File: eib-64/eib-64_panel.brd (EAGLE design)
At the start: 70.6 x 68 mm, 300 parts, among them J1 DF40-REC, J10 DF40-REC, J11 DF40-REC, J15 DF40-REC, J16 DF40-REC, J17 DF40-REC, J18 DF40-REC, J2 DF40-REC, J3 DF40-REC, J4 DF40-REC, J8 DF40-REC, J9 DF40-REC

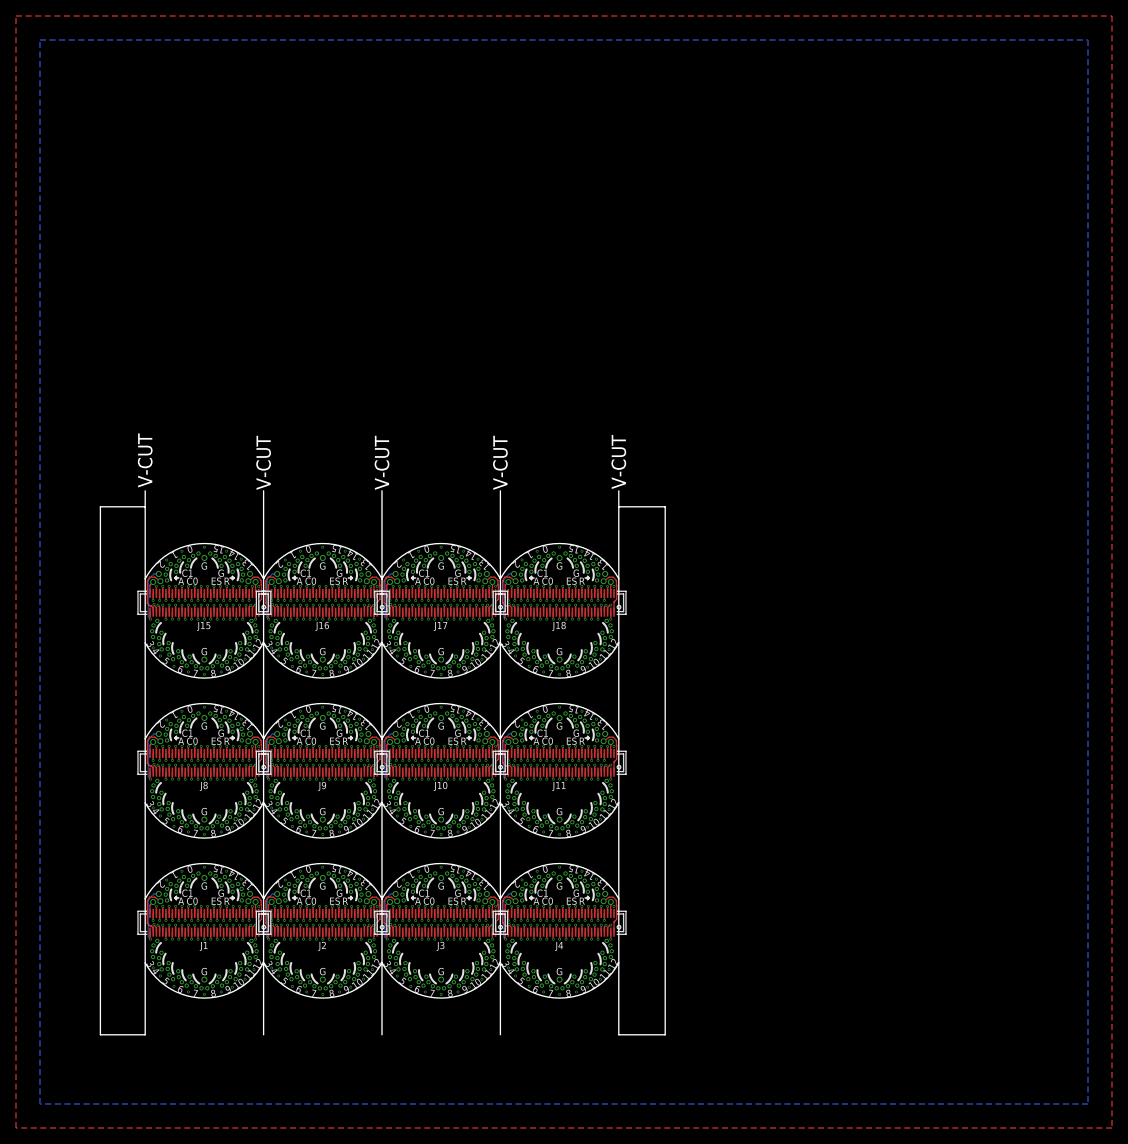
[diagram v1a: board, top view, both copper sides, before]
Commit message: eib-64 rev. 1.1
- Fits latest shuttle drive reatining feature.
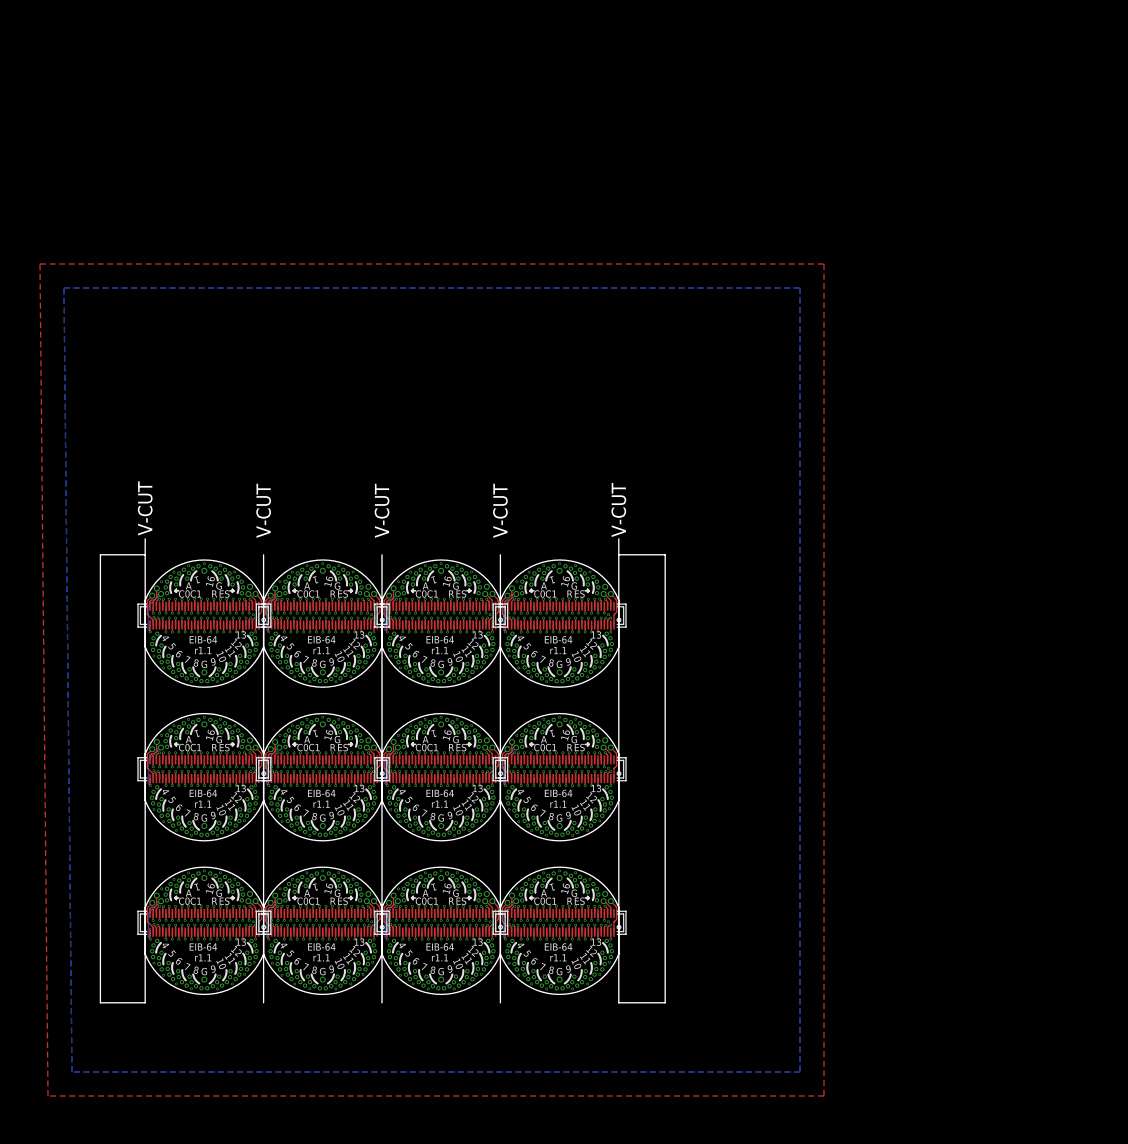
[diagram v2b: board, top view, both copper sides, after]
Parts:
- removed AN14, AN15, AN16, AN17, CAT28, CAT29, CAT30, CAT31, CAT32, CAT33, CAT34, CAT35, ESTIM14, ESTIM15, ESTIM16, ESTIM17, GND2, GND29, GND30, GND31, GND32, GND33, GND34, GND35, REF14, REF15, REF16, REF17, SHLD_A14, SHLD_A15, SHLD_A16, SHLD_A17: LRG_GP, jonnew:GOLDPIN_0.5ID_0.7OD
- removed J15, J16, J17, J18: DF40-REC, jonnew:DF40-70REC
- removed TET224, TET240, TET256, TET272: 0, jonnew:TETRODE_0.3ID_LINEAR_MOUSE
- removed TET225, TET241, TET257, TET273: 1, jonnew:TETRODE_0.3ID_LINEAR_MOUSE
- removed TET226, TET242, TET258, TET274: 2, jonnew:TETRODE_0.3ID_LINEAR_MOUSE
- removed TET227, TET243, TET259, TET275: 3, jonnew:TETRODE_0.3ID_LINEAR_MOUSE
- removed TET228, TET244, TET260, TET276: 4, jonnew:TETRODE_0.3ID_LINEAR_MOUSE
- removed TET229, TET245, TET261, TET277: 5, jonnew:TETRODE_0.3ID_LINEAR_MOUSE
- removed TET230, TET246, TET262, TET278: 6, jonnew:TETRODE_0.3ID_LINEAR_MOUSE
- removed TET231, TET247, TET263, TET279: 7, jonnew:TETRODE_0.3ID_LINEAR_MOUSE
- removed TET232, TET248, TET264, TET280: 15, jonnew:TETRODE_0.3ID_LINEAR_MOUSE
- removed TET233, TET249, TET265, TET281: 14, jonnew:TETRODE_0.3ID_LINEAR_MOUSE
- removed TET234, TET250, TET266, TET282: 13, jonnew:TETRODE_0.3ID_LINEAR_MOUSE
- removed TET235, TET251, TET267, TET283: 12, jonnew:TETRODE_0.3ID_LINEAR_MOUSE
- removed TET236, TET252, TET268, TET284: 11, jonnew:TETRODE_0.3ID_LINEAR_MOUSE
- removed TET237, TET253, TET269, TET285: 10, jonnew:TETRODE_0.3ID_LINEAR_MOUSE
- removed TET238, TET254, TET270, TET286: 9, jonnew:TETRODE_0.3ID_LINEAR_MOUSE
- removed TET239, TET255, TET271, TET287: 8, jonnew:TETRODE_0.3ID_LINEAR_MOUSE
- added AN11, AN4, AN5, AN6, CAT10, CAT11, CAT12, CAT13, CAT22, CAT23, CAT8, CAT9, ESTIM11, ESTIM4, ESTIM5, ESTIM6, GND10, GND11, GND12, GND13, GND22, GND23, GND8, GND9, REF11, REF4, REF5, REF6, SHLD_A11, SHLD_A4, SHLD_A5, SHLD_A6: LRG_GP, jonnew:GOLDPIN_0.5ID_0.7OD
- added J12, J5, J6, J7: DF40-REC, jonnew:DF40-70REC
- added TET100, TET180, TET68, TET84: 4, jonnew:TETRODE_0.3ID_LINEAR_MOUSE
- added TET101, TET181, TET69, TET85: 5, jonnew:TETRODE_0.3ID_LINEAR_MOUSE
- added TET102, TET182, TET70, TET86: 6, jonnew:TETRODE_0.3ID_LINEAR_MOUSE
- added TET103, TET183, TET71, TET87: 7, jonnew:TETRODE_0.3ID_LINEAR_MOUSE
- added TET104, TET184, TET72, TET88: 15, jonnew:TETRODE_0.3ID_LINEAR_MOUSE
- added TET105, TET185, TET73, TET89: 14, jonnew:TETRODE_0.3ID_LINEAR_MOUSE
- added TET106, TET186, TET74, TET90: 13, jonnew:TETRODE_0.3ID_LINEAR_MOUSE
- added TET107, TET187, TET75, TET91: 12, jonnew:TETRODE_0.3ID_LINEAR_MOUSE
- added TET108, TET188, TET76, TET92: 11, jonnew:TETRODE_0.3ID_LINEAR_MOUSE
- added TET109, TET189, TET77, TET93: 10, jonnew:TETRODE_0.3ID_LINEAR_MOUSE
- added TET110, TET190, TET78, TET94: 9, jonnew:TETRODE_0.3ID_LINEAR_MOUSE
- added TET111, TET191, TET79, TET95: 8, jonnew:TETRODE_0.3ID_LINEAR_MOUSE
- added TET176, TET64, TET80, TET96: 0, jonnew:TETRODE_0.3ID_LINEAR_MOUSE
- added TET177, TET65, TET81, TET97: 1, jonnew:TETRODE_0.3ID_LINEAR_MOUSE
- added TET178, TET66, TET82, TET98: 2, jonnew:TETRODE_0.3ID_LINEAR_MOUSE
- added TET179, TET67, TET83, TET99: 3, jonnew:TETRODE_0.3ID_LINEAR_MOUSE
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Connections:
- removed net AN14: AN14.P$1, J15.36
- removed net AN15: AN15.P$1, J16.36
- removed net AN16: AN16.P$1, J17.36
- removed net AN17: AN17.P$1, J18.36
- removed net CAT28: CAT28.P$1, J15.34
- removed net CAT29: CAT29.P$1, J15.35
- removed net CAT30: CAT30.P$1, J16.34
- removed net CAT31: CAT31.P$1, J16.35
- removed net CAT32: CAT32.P$1, J17.34
- removed net CAT33: CAT33.P$1, J17.35
- removed net CAT34: CAT34.P$1, J18.34
- removed net CAT35: CAT35.P$1, J18.35
- removed net ESTIM14: ESTIM14.P$1, J15.1
- removed net ESTIM15: ESTIM15.P$1, J16.1
- removed net ESTIM16: ESTIM16.P$1, J17.1
- removed net ESTIM17: ESTIM17.P$1, J18.1
- removed net N$1000: J16.55, TET248.1
- removed net N$1001: J16.54, TET248.2
- removed net N$1002: J16.53, TET248.3
- removed net N$1003: J16.52, TET240.3
- removed net N$1004: J16.51, TET240.2
- removed net N$1005: J16.50, TET240.1
- removed net N$1006: J16.49, TET240.0
- removed net N$1007: J16.48, TET241.3
- removed net N$1008: J16.47, TET241.2
- removed net N$1009: J16.46, TET241.1
- removed net N$1010: J16.45, TET241.0
- removed net N$1011: J16.44, TET242.3
- removed net N$1012: J16.43, TET242.2
- removed net N$1013: J16.42, TET242.1
- removed net N$1014: J16.41, TET242.0
- removed net N$1015: J16.40, TET243.0
- removed net N$1016: J16.38, TET243.2
- removed net N$1017: J16.5, TET252.3
- removed net N$1018: J16.4, TET252.2
- removed net N$1019: J16.3, TET252.1
- removed net N$1020: J16.2, TET252.0
- removed net N$1021: J16.65, TET251.2
- removed net N$1022: J16.67, TET251.0
- removed net N$1023: J16.39, TET243.3
- removed net N$1024: J16.37, TET243.1
- removed net N$1025: J17.33, TET260.0
- removed net N$1026: J17.32, TET260.1
- removed net N$1027: J17.31, TET260.2
- removed net N$1028: J17.30, TET260.3
- removed net N$1029: J17.29, TET261.0
- removed net N$1030: J17.28, TET261.1
- removed net N$1031: J17.27, TET261.2
- removed net N$1032: J17.26, TET261.3
- removed net N$1033: J17.25, TET262.0
- removed net N$1034: J17.24, TET262.1
- removed net N$1035: J17.23, TET262.2
- removed net N$1036: J17.22, TET262.3
- removed net N$1037: J17.21, TET263.0
- removed net N$1038: J17.20, TET263.1
- removed net N$1039: J17.19, TET263.2
- removed net N$1040: J17.18, TET263.3
- removed net N$1041: J17.17, TET271.3
- removed net N$1042: J17.16, TET271.2
- removed net N$1043: J17.15, TET271.1
- removed net N$1044: J17.14, TET271.0
- removed net N$1045: J17.13, TET270.3
- removed net N$1046: J17.12, TET270.2
- removed net N$1047: J17.11, TET270.1
- removed net N$1048: J17.10, TET270.0
- removed net N$1049: J17.9, TET269.3
- removed net N$1050: J17.8, TET269.2
- removed net N$1051: J17.7, TET269.1
- removed net N$1052: J17.6, TET269.0
- removed net N$1053: J17.68, TET267.3
- removed net N$1054: J17.66, TET267.1
- removed net N$1055: J17.64, TET266.0
- removed net N$1056: J17.63, TET266.1
- removed net N$1057: J17.62, TET266.2
- removed net N$1058: J17.61, TET266.3
- removed net N$1059: J17.60, TET265.0
- removed net N$1060: J17.59, TET265.1
- removed net N$1061: J17.58, TET265.2
- removed net N$1062: J17.57, TET265.3
- removed net N$1063: J17.56, TET264.0
- removed net N$1064: J17.55, TET264.1
- removed net N$1065: J17.54, TET264.2
- removed net N$1066: J17.53, TET264.3
- removed net N$1067: J17.52, TET256.3
- removed net N$1068: J17.51, TET256.2
- removed net N$1069: J17.50, TET256.1
- removed net N$1070: J17.49, TET256.0
- removed net N$1071: J17.48, TET257.3
- removed net N$1072: J17.47, TET257.2
- removed net N$1073: J17.46, TET257.1
- removed net N$1074: J17.45, TET257.0
- removed net N$1075: J17.44, TET258.3
- removed net N$1076: J17.43, TET258.2
- removed net N$1077: J17.42, TET258.1
- removed net N$1078: J17.41, TET258.0
- removed net N$1079: J17.40, TET259.0
- removed net N$1080: J17.38, TET259.2
- removed net N$1081: J17.5, TET268.3
- removed net N$1082: J17.4, TET268.2
- removed net N$1083: J17.3, TET268.1
- removed net N$1084: J17.2, TET268.0
- removed net N$1085: J17.65, TET267.2
- removed net N$1086: J17.67, TET267.0
- removed net N$1087: J17.39, TET259.3
- removed net N$1088: J17.37, TET259.1
- removed net N$1089: J18.33, TET276.0
- removed net N$1090: J18.32, TET276.1
- removed net N$1091: J18.31, TET276.2
- removed net N$1092: J18.30, TET276.3
- removed net N$1093: J18.29, TET277.0
- removed net N$1094: J18.28, TET277.1
- removed net N$1095: J18.27, TET277.2
- removed net N$1096: J18.26, TET277.3
- removed net N$1097: J18.25, TET278.0
- removed net N$1098: J18.24, TET278.1
- removed net N$1099: J18.23, TET278.2
- removed net N$1100: J18.22, TET278.3
- removed net N$1101: J18.21, TET279.0
- removed net N$1102: J18.20, TET279.1
- removed net N$1103: J18.19, TET279.2
- removed net N$1104: J18.18, TET279.3
- removed net N$1105: J18.17, TET287.3
- removed net N$1106: J18.16, TET287.2
- removed net N$1107: J18.15, TET287.1
- removed net N$1108: J18.14, TET287.0
- removed net N$1109: J18.13, TET286.3
- removed net N$1110: J18.12, TET286.2
- removed net N$1111: J18.11, TET286.1
- removed net N$1112: J18.10, TET286.0
- removed net N$1113: J18.9, TET285.3
- removed net N$1114: J18.8, TET285.2
- removed net N$1115: J18.7, TET285.1
- removed net N$1116: J18.6, TET285.0
- removed net N$1117: J18.68, TET283.3
- removed net N$1118: J18.66, TET283.1
- removed net N$1119: J18.64, TET282.0
- removed net N$1120: J18.63, TET282.1
- removed net N$1121: J18.62, TET282.2
- removed net N$1122: J18.61, TET282.3
- removed net N$1123: J18.60, TET281.0
- removed net N$1124: J18.59, TET281.1
- removed net N$1125: J18.58, TET281.2
- removed net N$1126: J18.57, TET281.3
- removed net N$1127: J18.56, TET280.0
- removed net N$1128: J18.55, TET280.1
- removed net N$1129: J18.54, TET280.2
- removed net N$1130: J18.53, TET280.3
- removed net N$1131: J18.52, TET272.3
- removed net N$1132: J18.51, TET272.2
- removed net N$1133: J18.50, TET272.1
- removed net N$1134: J18.49, TET272.0
- removed net N$1135: J18.48, TET273.3
- removed net N$1136: J18.47, TET273.2
- removed net N$1137: J18.46, TET273.1
- removed net N$1138: J18.45, TET273.0
- removed net N$1139: J18.44, TET274.3
- removed net N$1140: J18.43, TET274.2
- removed net N$1141: J18.42, TET274.1
- removed net N$1142: J18.41, TET274.0
- removed net N$1143: J18.40, TET275.0
- removed net N$1144: J18.38, TET275.2
- removed net N$1145: J18.5, TET284.3
- removed net N$1146: J18.4, TET284.2
- removed net N$1147: J18.3, TET284.1
- removed net N$1148: J18.2, TET284.0
- removed net N$1149: J18.65, TET283.2
- removed net N$1150: J18.67, TET283.0
- removed net N$1151: J18.39, TET275.3
- removed net N$1152: J18.37, TET275.1
- removed net N$897: J15.33, TET228.0
- removed net N$898: J15.32, TET228.1
- removed net N$899: J15.31, TET228.2
- removed net N$900: J15.30, TET228.3
- removed net N$901: J15.29, TET229.0
- removed net N$902: J15.28, TET229.1
- removed net N$903: J15.27, TET229.2
- removed net N$904: J15.26, TET229.3
- removed net N$905: J15.25, TET230.0
- removed net N$906: J15.24, TET230.1
- removed net N$907: J15.23, TET230.2
- removed net N$908: J15.22, TET230.3
- removed net N$909: J15.21, TET231.0
- removed net N$910: J15.20, TET231.1
- removed net N$911: J15.19, TET231.2
- removed net N$912: J15.18, TET231.3
- removed net N$913: J15.17, TET239.3
- removed net N$914: J15.16, TET239.2
- removed net N$915: J15.15, TET239.1
- removed net N$916: J15.14, TET239.0
- removed net N$917: J15.13, TET238.3
- removed net N$918: J15.12, TET238.2
- removed net N$919: J15.11, TET238.1
- removed net N$920: J15.10, TET238.0
- removed net N$921: J15.9, TET237.3
- removed net N$922: J15.8, TET237.2
- removed net N$923: J15.7, TET237.1
- removed net N$924: J15.6, TET237.0
- removed net N$925: J15.68, TET235.3
- removed net N$926: J15.66, TET235.1
- removed net N$927: J15.64, TET234.0
- removed net N$928: J15.63, TET234.1
- removed net N$929: J15.62, TET234.2
- removed net N$930: J15.61, TET234.3
- removed net N$931: J15.60, TET233.0
- removed net N$932: J15.59, TET233.1
- removed net N$933: J15.58, TET233.2
- removed net N$934: J15.57, TET233.3
- removed net N$935: J15.56, TET232.0
- removed net N$936: J15.55, TET232.1
- removed net N$937: J15.54, TET232.2
- removed net N$938: J15.53, TET232.3
- removed net N$939: J15.52, TET224.3
- removed net N$940: J15.51, TET224.2
- removed net N$941: J15.50, TET224.1
- removed net N$942: J15.49, TET224.0
- removed net N$943: J15.48, TET225.3
- removed net N$944: J15.47, TET225.2
- removed net N$945: J15.46, TET225.1
- removed net N$946: J15.45, TET225.0
- removed net N$947: J15.44, TET226.3
- removed net N$948: J15.43, TET226.2
- removed net N$949: J15.42, TET226.1
- removed net N$950: J15.41, TET226.0
- removed net N$951: J15.40, TET227.0
- removed net N$952: J15.38, TET227.2
- removed net N$953: J15.5, TET236.3
- removed net N$954: J15.4, TET236.2
- removed net N$955: J15.3, TET236.1
- removed net N$956: J15.2, TET236.0
- removed net N$957: J15.65, TET235.2
- removed net N$958: J15.67, TET235.0
- removed net N$959: J15.39, TET227.3
- removed net N$960: J15.37, TET227.1
- removed net N$961: J16.33, TET244.0
- removed net N$962: J16.32, TET244.1
- removed net N$963: J16.31, TET244.2
- removed net N$964: J16.30, TET244.3
- removed net N$965: J16.29, TET245.0
- removed net N$966: J16.28, TET245.1
- removed net N$967: J16.27, TET245.2
- removed net N$968: J16.26, TET245.3
- removed net N$969: J16.25, TET246.0
- removed net N$970: J16.24, TET246.1
- removed net N$971: J16.23, TET246.2
- removed net N$972: J16.22, TET246.3
- removed net N$973: J16.21, TET247.0
- removed net N$974: J16.20, TET247.1
- removed net N$975: J16.19, TET247.2
- removed net N$976: J16.18, TET247.3
- removed net N$977: J16.17, TET255.3
- removed net N$978: J16.16, TET255.2
- removed net N$979: J16.15, TET255.1
- removed net N$980: J16.14, TET255.0
- removed net N$981: J16.13, TET254.3
- removed net N$982: J16.12, TET254.2
- removed net N$983: J16.11, TET254.1
- removed net N$984: J16.10, TET254.0
- removed net N$985: J16.9, TET253.3
- removed net N$986: J16.8, TET253.2
- removed net N$987: J16.7, TET253.1
- removed net N$988: J16.6, TET253.0
- removed net N$989: J16.68, TET251.3
- removed net N$990: J16.66, TET251.1
- removed net N$991: J16.64, TET250.0
- removed net N$992: J16.63, TET250.1
- removed net N$993: J16.62, TET250.2
- removed net N$994: J16.61, TET250.3
- removed net N$995: J16.60, TET249.0
- removed net N$996: J16.59, TET249.1
- removed net N$997: J16.58, TET249.2
- removed net N$998: J16.57, TET249.3
- removed net N$999: J16.56, TET248.0
- removed net REF14: J15.69, REF14.P$1
- removed net REF15: J16.69, REF15.P$1
- removed net REF16: J17.69, REF16.P$1
- removed net REF17: J18.69, REF17.P$1
- new net AN11: AN11.P$1, J12.36
- new net AN4: AN4.P$1, J5.36
- new net AN5: AN5.P$1, J6.36
- new net AN6: AN6.P$1, J7.36
- new net CAT10: CAT10.P$1, J6.34
- new net CAT11: CAT11.P$1, J6.35
- new net CAT12: CAT12.P$1, J7.34
- new net CAT13: CAT13.P$1, J7.35
- new net CAT22: CAT22.P$1, J12.34
- new net CAT23: CAT23.P$1, J12.35
- new net CAT8: CAT8.P$1, J5.34
- new net CAT9: CAT9.P$1, J5.35
- new net ESTIM11: ESTIM11.P$1, J12.1
- new net ESTIM4: ESTIM4.P$1, J5.1
- new net ESTIM5: ESTIM5.P$1, J6.1
- new net ESTIM6: ESTIM6.P$1, J7.1
- new net N$257: J5.33, TET68.0
- new net N$258: J5.32, TET68.1
- new net N$259: J5.31, TET68.2
- new net N$260: J5.30, TET68.3
- new net N$261: J5.29, TET69.0
- new net N$262: J5.28, TET69.1
- new net N$263: J5.27, TET69.2
- new net N$264: J5.26, TET69.3
- new net N$265: J5.25, TET70.0
- new net N$266: J5.24, TET70.1
- new net N$267: J5.23, TET70.2
- new net N$268: J5.22, TET70.3
- new net N$269: J5.21, TET71.0
- new net N$270: J5.20, TET71.1
- new net N$271: J5.19, TET71.2
- new net N$272: J5.18, TET71.3
- new net N$273: J5.17, TET79.3
- new net N$274: J5.16, TET79.2
- new net N$275: J5.15, TET79.1
- new net N$276: J5.14, TET79.0
- new net N$277: J5.13, TET78.3
- new net N$278: J5.12, TET78.2
- new net N$279: J5.11, TET78.1
- new net N$280: J5.10, TET78.0
- new net N$281: J5.9, TET77.3
- new net N$282: J5.8, TET77.2
- new net N$283: J5.7, TET77.1
- new net N$284: J5.6, TET77.0
- new net N$285: J5.68, TET75.3
- new net N$286: J5.66, TET75.1
- new net N$287: J5.64, TET74.0
- new net N$288: J5.63, TET74.1
- new net N$289: J5.62, TET74.2
- new net N$290: J5.61, TET74.3
- new net N$291: J5.60, TET73.0
- new net N$292: J5.59, TET73.1
- new net N$293: J5.58, TET73.2
- new net N$294: J5.57, TET73.3
- new net N$295: J5.56, TET72.0
- new net N$296: J5.55, TET72.1
- new net N$297: J5.54, TET72.2
- new net N$298: J5.53, TET72.3
- new net N$299: J5.52, TET64.3
- new net N$300: J5.51, TET64.2
- new net N$301: J5.50, TET64.1
- new net N$302: J5.49, TET64.0
- new net N$303: J5.48, TET65.3
- new net N$304: J5.47, TET65.2
- new net N$305: J5.46, TET65.1
- new net N$306: J5.45, TET65.0
- new net N$307: J5.44, TET66.3
- new net N$308: J5.43, TET66.2
- new net N$309: J5.42, TET66.1
- new net N$310: J5.41, TET66.0
- new net N$311: J5.40, TET67.0
- new net N$312: J5.38, TET67.2
- new net N$313: J5.5, TET76.3
- new net N$314: J5.4, TET76.2
- new net N$315: J5.3, TET76.1
- new net N$316: J5.2, TET76.0
- new net N$317: J5.65, TET75.2
- new net N$318: J5.67, TET75.0
- new net N$319: J5.39, TET67.3
- new net N$320: J5.37, TET67.1
- new net N$321: J6.33, TET84.0
- new net N$322: J6.32, TET84.1
- new net N$323: J6.31, TET84.2
- new net N$324: J6.30, TET84.3
- new net N$325: J6.29, TET85.0
- new net N$326: J6.28, TET85.1
- new net N$327: J6.27, TET85.2
- new net N$328: J6.26, TET85.3
- new net N$329: J6.25, TET86.0
- new net N$330: J6.24, TET86.1
- new net N$331: J6.23, TET86.2
- new net N$332: J6.22, TET86.3
- new net N$333: J6.21, TET87.0
- new net N$334: J6.20, TET87.1
- new net N$335: J6.19, TET87.2
- new net N$336: J6.18, TET87.3
- new net N$337: J6.17, TET95.3
- new net N$338: J6.16, TET95.2
- new net N$339: J6.15, TET95.1
- new net N$340: J6.14, TET95.0
- new net N$341: J6.13, TET94.3
- new net N$342: J6.12, TET94.2
- new net N$343: J6.11, TET94.1
- new net N$344: J6.10, TET94.0
- new net N$345: J6.9, TET93.3
- new net N$346: J6.8, TET93.2
- new net N$347: J6.7, TET93.1
- new net N$348: J6.6, TET93.0
- new net N$349: J6.68, TET91.3
- new net N$350: J6.66, TET91.1
- new net N$351: J6.64, TET90.0
- new net N$352: J6.63, TET90.1
- new net N$353: J6.62, TET90.2
- new net N$354: J6.61, TET90.3
- new net N$355: J6.60, TET89.0
- new net N$356: J6.59, TET89.1
- new net N$357: J6.58, TET89.2
- new net N$358: J6.57, TET89.3
- new net N$359: J6.56, TET88.0
- new net N$360: J6.55, TET88.1
- new net N$361: J6.54, TET88.2
- new net N$362: J6.53, TET88.3
- new net N$363: J6.52, TET80.3
- new net N$364: J6.51, TET80.2
- new net N$365: J6.50, TET80.1
- new net N$366: J6.49, TET80.0
- new net N$367: J6.48, TET81.3
- new net N$368: J6.47, TET81.2
- new net N$369: J6.46, TET81.1
- new net N$370: J6.45, TET81.0
- new net N$371: J6.44, TET82.3
- new net N$372: J6.43, TET82.2
- new net N$373: J6.42, TET82.1
- new net N$374: J6.41, TET82.0
- new net N$375: J6.40, TET83.0
- new net N$376: J6.38, TET83.2
- new net N$377: J6.5, TET92.3
- new net N$378: J6.4, TET92.2
- new net N$379: J6.3, TET92.1
- new net N$380: J6.2, TET92.0
- new net N$381: J6.65, TET91.2
- new net N$382: J6.67, TET91.0
- new net N$383: J6.39, TET83.3
- new net N$384: J6.37, TET83.1
- new net N$385: J7.33, TET100.0
- new net N$386: J7.32, TET100.1
- new net N$387: J7.31, TET100.2
- new net N$388: J7.30, TET100.3
- new net N$389: J7.29, TET101.0
- new net N$390: J7.28, TET101.1
- new net N$391: J7.27, TET101.2
- new net N$392: J7.26, TET101.3
- new net N$393: J7.25, TET102.0
- new net N$394: J7.24, TET102.1
- new net N$395: J7.23, TET102.2
- new net N$396: J7.22, TET102.3
- new net N$397: J7.21, TET103.0
- new net N$398: J7.20, TET103.1
- new net N$399: J7.19, TET103.2
- new net N$400: J7.18, TET103.3
- new net N$401: J7.17, TET111.3
- new net N$402: J7.16, TET111.2
- new net N$403: J7.15, TET111.1
- new net N$404: J7.14, TET111.0
- new net N$405: J7.13, TET110.3
- new net N$406: J7.12, TET110.2
- new net N$407: J7.11, TET110.1
- new net N$408: J7.10, TET110.0
- new net N$409: J7.9, TET109.3
- new net N$410: J7.8, TET109.2
- new net N$411: J7.7, TET109.1
- new net N$412: J7.6, TET109.0
- new net N$413: J7.68, TET107.3
- new net N$414: J7.66, TET107.1
- new net N$415: J7.64, TET106.0
- new net N$416: J7.63, TET106.1
- new net N$417: J7.62, TET106.2
- new net N$418: J7.61, TET106.3
- new net N$419: J7.60, TET105.0
- new net N$420: J7.59, TET105.1
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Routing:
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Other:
- board size 70.6 x 68 mm -> 70.6 x 58 mm
- board text added: "16"
- board text added: "EIB-64 r1.1"
- board text removed: "0"
- board text removed: "14"
- board text removed: "15"
- board text removed: "2"
- board text removed: "3"

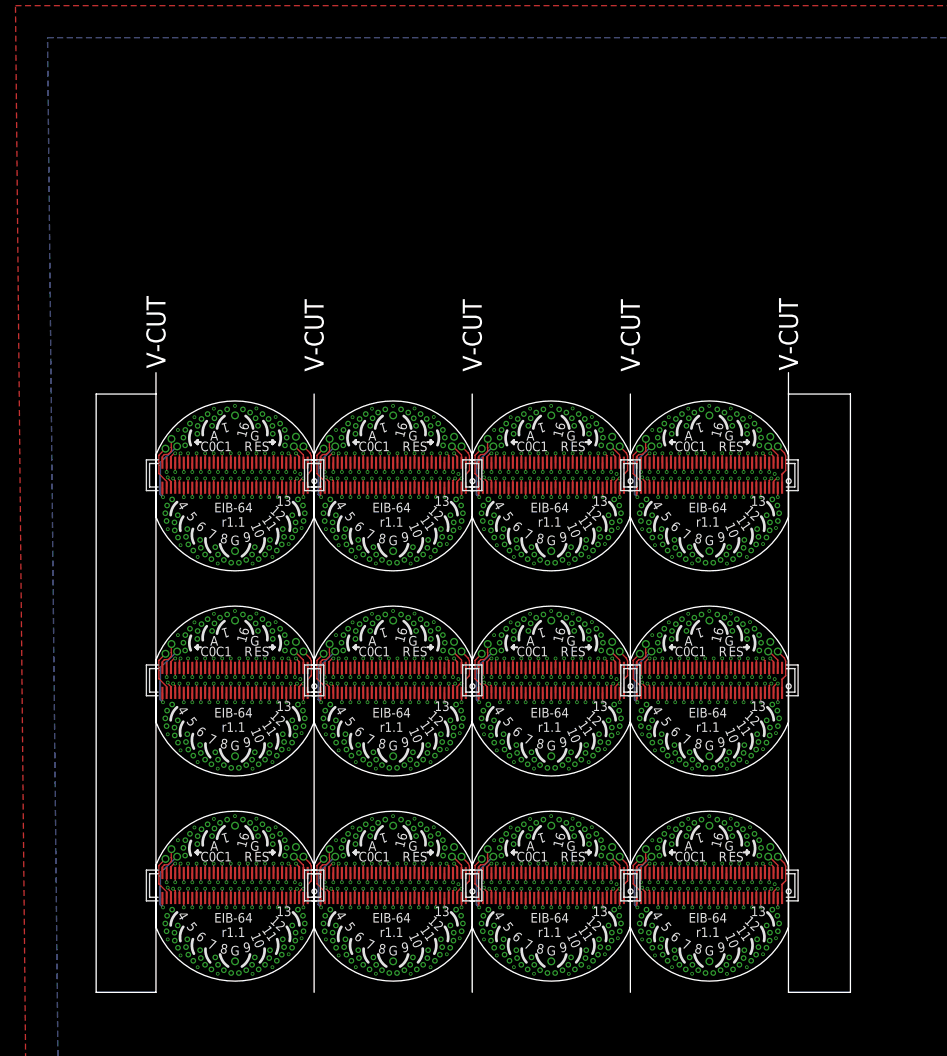
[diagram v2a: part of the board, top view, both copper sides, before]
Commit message: Increased size of eib-64 panel
- To fit minimal requirement of 7cm x 7cm for JLCPCB
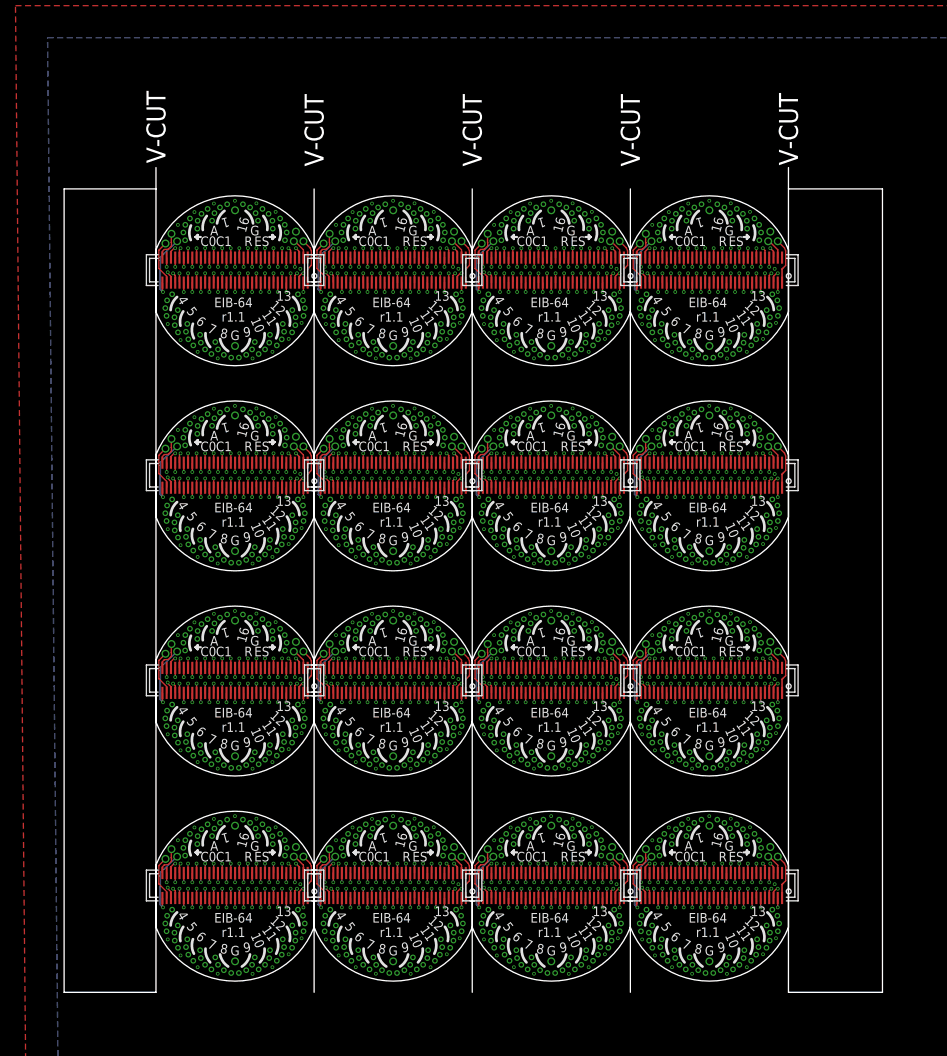
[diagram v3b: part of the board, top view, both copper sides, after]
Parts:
- added AN12, AN13, AN14, AN15, CAT24, CAT25, CAT26, CAT27, CAT28, CAT29, CAT30, CAT31, ESTIM12, ESTIM13, ESTIM14, ESTIM15, GND2, GND24, GND25, GND26, GND27, GND28, GND29, GND30, REF12, REF13, REF14, REF15, SHLD_A12, SHLD_A13, SHLD_A14, SHLD_A15: LRG_GP, jonnew:GOLDPIN_0.5ID_0.7OD
- added J13, J14, J15, J16: DF40-REC, jonnew:DF40-70REC
- added TET192, TET208, TET224, TET240: 0, jonnew:TETRODE_0.3ID_LINEAR_MOUSE
- added TET193, TET209, TET225, TET241: 1, jonnew:TETRODE_0.3ID_LINEAR_MOUSE
- added TET194, TET210, TET226, TET242: 2, jonnew:TETRODE_0.3ID_LINEAR_MOUSE
- added TET195, TET211, TET227, TET243: 3, jonnew:TETRODE_0.3ID_LINEAR_MOUSE
- added TET196, TET212, TET228, TET244: 4, jonnew:TETRODE_0.3ID_LINEAR_MOUSE
- added TET197, TET213, TET229, TET245: 5, jonnew:TETRODE_0.3ID_LINEAR_MOUSE
- added TET198, TET214, TET230, TET246: 6, jonnew:TETRODE_0.3ID_LINEAR_MOUSE
- added TET199, TET215, TET231, TET247: 7, jonnew:TETRODE_0.3ID_LINEAR_MOUSE
- added TET200, TET216, TET232, TET248: 15, jonnew:TETRODE_0.3ID_LINEAR_MOUSE
- added TET201, TET217, TET233, TET249: 14, jonnew:TETRODE_0.3ID_LINEAR_MOUSE
- added TET202, TET218, TET234, TET250: 13, jonnew:TETRODE_0.3ID_LINEAR_MOUSE
- added TET203, TET219, TET235, TET251: 12, jonnew:TETRODE_0.3ID_LINEAR_MOUSE
- added TET204, TET220, TET236, TET252: 11, jonnew:TETRODE_0.3ID_LINEAR_MOUSE
- added TET205, TET221, TET237, TET253: 10, jonnew:TETRODE_0.3ID_LINEAR_MOUSE
- added TET206, TET222, TET238, TET254: 9, jonnew:TETRODE_0.3ID_LINEAR_MOUSE
- added TET207, TET223, TET239, TET255: 8, jonnew:TETRODE_0.3ID_LINEAR_MOUSE
- moved AN10 19.2 mm to (23.6, 62.0)
- moved AN11 19.2 mm to (38.5, 62.0)
- moved AN8 19.2 mm to (-5.95, 62.0)
- moved AN9 19.2 mm to (8.85, 62.0)
- moved CAT16 19.2 mm to (-6.51, 61.1)
- moved CAT18 19.2 mm to (8.29, 61.1)
- moved CAT20 19.2 mm to (23.1, 61.1)
- moved CAT22 19.2 mm to (37.9, 61.1)
- moved GND16 19.2 mm to (0.00, 64.2)
- moved GND17 19.2 mm to (0.00, 51.5)
- moved GND18 19.2 mm to (14.8, 64.2)
- moved GND19 19.2 mm to (14.8, 51.5)
- moved GND20 19.2 mm to (29.6, 64.2)
- moved GND21 19.2 mm to (29.6, 51.5)
- moved GND22 19.2 mm to (44.4, 64.2)
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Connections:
- new net AN12: AN12.P$1, J13.36
- new net AN13: AN13.P$1, J14.36
- new net AN14: AN14.P$1, J15.36
- new net AN15: AN15.P$1, J16.36
- new net CAT24: CAT24.P$1, J13.34
- new net CAT25: CAT25.P$1, J13.35
- new net CAT26: CAT26.P$1, J14.34
- new net CAT27: CAT27.P$1, J14.35
- new net CAT28: CAT28.P$1, J15.34
- new net CAT29: CAT29.P$1, J15.35
- new net CAT30: CAT30.P$1, J16.34
- new net CAT31: CAT31.P$1, J16.35
- new net ESTIM12: ESTIM12.P$1, J13.1
- new net ESTIM13: ESTIM13.P$1, J14.1
- new net ESTIM14: ESTIM14.P$1, J15.1
- new net ESTIM15: ESTIM15.P$1, J16.1
- new net N$1000: J16.55, TET248.1
- new net N$1001: J16.54, TET248.2
- new net N$1002: J16.53, TET248.3
- new net N$1003: J16.52, TET240.3
- new net N$1004: J16.51, TET240.2
- new net N$1005: J16.50, TET240.1
- new net N$1006: J16.49, TET240.0
- new net N$1007: J16.48, TET241.3
- new net N$1008: J16.47, TET241.2
- new net N$1009: J16.46, TET241.1
- new net N$1010: J16.45, TET241.0
- new net N$1011: J16.44, TET242.3
- new net N$1012: J16.43, TET242.2
- new net N$1013: J16.42, TET242.1
- new net N$1014: J16.41, TET242.0
- new net N$1015: J16.40, TET243.0
- new net N$1016: J16.38, TET243.2
- new net N$1017: J16.5, TET252.3
- new net N$1018: J16.4, TET252.2
- new net N$1019: J16.3, TET252.1
- new net N$1020: J16.2, TET252.0
- new net N$1021: J16.65, TET251.2
- new net N$1022: J16.67, TET251.0
- new net N$1023: J16.39, TET243.3
- new net N$1024: J16.37, TET243.1
- new net N$769: J13.33, TET196.0
- new net N$770: J13.32, TET196.1
- new net N$771: J13.31, TET196.2
- new net N$772: J13.30, TET196.3
- new net N$773: J13.29, TET197.0
- new net N$774: J13.28, TET197.1
- new net N$775: J13.27, TET197.2
- new net N$776: J13.26, TET197.3
- new net N$777: J13.25, TET198.0
- new net N$778: J13.24, TET198.1
- new net N$779: J13.23, TET198.2
- new net N$780: J13.22, TET198.3
- new net N$781: J13.21, TET199.0
- new net N$782: J13.20, TET199.1
- new net N$783: J13.19, TET199.2
- new net N$784: J13.18, TET199.3
- new net N$785: J13.17, TET207.3
- new net N$786: J13.16, TET207.2
- new net N$787: J13.15, TET207.1
- new net N$788: J13.14, TET207.0
- new net N$789: J13.13, TET206.3
- new net N$790: J13.12, TET206.2
- new net N$791: J13.11, TET206.1
- new net N$792: J13.10, TET206.0
- new net N$793: J13.9, TET205.3
- new net N$794: J13.8, TET205.2
- new net N$795: J13.7, TET205.1
- new net N$796: J13.6, TET205.0
- new net N$797: J13.68, TET203.3
- new net N$798: J13.66, TET203.1
- new net N$799: J13.64, TET202.0
- new net N$800: J13.63, TET202.1
- new net N$801: J13.62, TET202.2
- new net N$802: J13.61, TET202.3
- new net N$803: J13.60, TET201.0
- new net N$804: J13.59, TET201.1
- new net N$805: J13.58, TET201.2
- new net N$806: J13.57, TET201.3
- new net N$807: J13.56, TET200.0
- new net N$808: J13.55, TET200.1
- new net N$809: J13.54, TET200.2
- new net N$810: J13.53, TET200.3
- new net N$811: J13.52, TET192.3
- new net N$812: J13.51, TET192.2
- new net N$813: J13.50, TET192.1
- new net N$814: J13.49, TET192.0
- new net N$815: J13.48, TET193.3
- new net N$816: J13.47, TET193.2
- new net N$817: J13.46, TET193.1
- new net N$818: J13.45, TET193.0
- new net N$819: J13.44, TET194.3
- new net N$820: J13.43, TET194.2
- new net N$821: J13.42, TET194.1
- new net N$822: J13.41, TET194.0
- new net N$823: J13.40, TET195.0
- new net N$824: J13.38, TET195.2
- new net N$825: J13.5, TET204.3
- new net N$826: J13.4, TET204.2
- new net N$827: J13.3, TET204.1
- new net N$828: J13.2, TET204.0
- new net N$829: J13.65, TET203.2
- new net N$830: J13.67, TET203.0
- new net N$831: J13.39, TET195.3
- new net N$832: J13.37, TET195.1
- new net N$833: J14.33, TET212.0
- new net N$834: J14.32, TET212.1
- new net N$835: J14.31, TET212.2
- new net N$836: J14.30, TET212.3
- new net N$837: J14.29, TET213.0
- new net N$838: J14.28, TET213.1
- new net N$839: J14.27, TET213.2
- new net N$840: J14.26, TET213.3
- new net N$841: J14.25, TET214.0
- new net N$842: J14.24, TET214.1
- new net N$843: J14.23, TET214.2
- new net N$844: J14.22, TET214.3
- new net N$845: J14.21, TET215.0
- new net N$846: J14.20, TET215.1
- new net N$847: J14.19, TET215.2
- new net N$848: J14.18, TET215.3
- new net N$849: J14.17, TET223.3
- new net N$850: J14.16, TET223.2
- new net N$851: J14.15, TET223.1
- new net N$852: J14.14, TET223.0
- new net N$853: J14.13, TET222.3
- new net N$854: J14.12, TET222.2
- new net N$855: J14.11, TET222.1
- new net N$856: J14.10, TET222.0
- new net N$857: J14.9, TET221.3
- new net N$858: J14.8, TET221.2
- new net N$859: J14.7, TET221.1
- new net N$860: J14.6, TET221.0
- new net N$861: J14.68, TET219.3
- new net N$862: J14.66, TET219.1
- new net N$863: J14.64, TET218.0
- new net N$864: J14.63, TET218.1
- new net N$865: J14.62, TET218.2
- new net N$866: J14.61, TET218.3
- new net N$867: J14.60, TET217.0
- new net N$868: J14.59, TET217.1
- new net N$869: J14.58, TET217.2
- new net N$870: J14.57, TET217.3
- new net N$871: J14.56, TET216.0
- new net N$872: J14.55, TET216.1
- new net N$873: J14.54, TET216.2
- new net N$874: J14.53, TET216.3
- new net N$875: J14.52, TET208.3
- new net N$876: J14.51, TET208.2
- new net N$877: J14.50, TET208.1
- new net N$878: J14.49, TET208.0
- new net N$879: J14.48, TET209.3
- new net N$880: J14.47, TET209.2
- new net N$881: J14.46, TET209.1
- new net N$882: J14.45, TET209.0
- new net N$883: J14.44, TET210.3
- new net N$884: J14.43, TET210.2
- new net N$885: J14.42, TET210.1
- new net N$886: J14.41, TET210.0
- new net N$887: J14.40, TET211.0
- new net N$888: J14.38, TET211.2
- new net N$889: J14.5, TET220.3
- new net N$890: J14.4, TET220.2
- new net N$891: J14.3, TET220.1
- new net N$892: J14.2, TET220.0
- new net N$893: J14.65, TET219.2
- new net N$894: J14.67, TET219.0
- new net N$895: J14.39, TET211.3
- new net N$896: J14.37, TET211.1
- new net N$897: J15.33, TET228.0
- new net N$898: J15.32, TET228.1
- new net N$899: J15.31, TET228.2
- new net N$900: J15.30, TET228.3
- new net N$901: J15.29, TET229.0
- new net N$902: J15.28, TET229.1
- new net N$903: J15.27, TET229.2
- new net N$904: J15.26, TET229.3
- new net N$905: J15.25, TET230.0
- new net N$906: J15.24, TET230.1
- new net N$907: J15.23, TET230.2
- new net N$908: J15.22, TET230.3
- new net N$909: J15.21, TET231.0
- new net N$910: J15.20, TET231.1
- new net N$911: J15.19, TET231.2
- new net N$912: J15.18, TET231.3
- new net N$913: J15.17, TET239.3
- new net N$914: J15.16, TET239.2
- new net N$915: J15.15, TET239.1
- new net N$916: J15.14, TET239.0
- new net N$917: J15.13, TET238.3
- new net N$918: J15.12, TET238.2
- new net N$919: J15.11, TET238.1
- new net N$920: J15.10, TET238.0
- new net N$921: J15.9, TET237.3
- new net N$922: J15.8, TET237.2
- new net N$923: J15.7, TET237.1
- new net N$924: J15.6, TET237.0
- new net N$925: J15.68, TET235.3
- new net N$926: J15.66, TET235.1
- new net N$927: J15.64, TET234.0
- new net N$928: J15.63, TET234.1
- new net N$929: J15.62, TET234.2
- new net N$930: J15.61, TET234.3
- new net N$931: J15.60, TET233.0
- new net N$932: J15.59, TET233.1
- new net N$933: J15.58, TET233.2
- new net N$934: J15.57, TET233.3
- new net N$935: J15.56, TET232.0
- new net N$936: J15.55, TET232.1
- new net N$937: J15.54, TET232.2
- new net N$938: J15.53, TET232.3
- new net N$939: J15.52, TET224.3
- new net N$940: J15.51, TET224.2
- new net N$941: J15.50, TET224.1
- new net N$942: J15.49, TET224.0
- new net N$943: J15.48, TET225.3
- new net N$944: J15.47, TET225.2
- new net N$945: J15.46, TET225.1
- new net N$946: J15.45, TET225.0
- new net N$947: J15.44, TET226.3
- new net N$948: J15.43, TET226.2
- new net N$949: J15.42, TET226.1
- new net N$950: J15.41, TET226.0
- new net N$951: J15.40, TET227.0
- new net N$952: J15.38, TET227.2
- new net N$953: J15.5, TET236.3
- new net N$954: J15.4, TET236.2
- new net N$955: J15.3, TET236.1
- new net N$956: J15.2, TET236.0
- new net N$957: J15.65, TET235.2
- new net N$958: J15.67, TET235.0
- new net N$959: J15.39, TET227.3
- new net N$960: J15.37, TET227.1
- new net N$961: J16.33, TET244.0
- new net N$962: J16.32, TET244.1
- new net N$963: J16.31, TET244.2
- new net N$964: J16.30, TET244.3
- new net N$965: J16.29, TET245.0
- new net N$966: J16.28, TET245.1
- new net N$967: J16.27, TET245.2
- new net N$968: J16.26, TET245.3
- new net N$969: J16.25, TET246.0
- new net N$970: J16.24, TET246.1
- new net N$971: J16.23, TET246.2
- new net N$972: J16.22, TET246.3
- new net N$973: J16.21, TET247.0
- new net N$974: J16.20, TET247.1
- new net N$975: J16.19, TET247.2
- new net N$976: J16.18, TET247.3
- new net N$977: J16.17, TET255.3
- new net N$978: J16.16, TET255.2
- new net N$979: J16.15, TET255.1
- new net N$980: J16.14, TET255.0
- new net N$981: J16.13, TET254.3
- new net N$982: J16.12, TET254.2
- new net N$983: J16.11, TET254.1
- new net N$984: J16.10, TET254.0
- new net N$985: J16.9, TET253.3
- new net N$986: J16.8, TET253.2
- new net N$987: J16.7, TET253.1
- new net N$988: J16.6, TET253.0
- new net N$989: J16.68, TET251.3
- new net N$990: J16.66, TET251.1
- new net N$991: J16.64, TET250.0
- new net N$992: J16.63, TET250.1
- new net N$993: J16.62, TET250.2
- new net N$994: J16.61, TET250.3
- new net N$995: J16.60, TET249.0
- new net N$996: J16.59, TET249.1
- new net N$997: J16.58, TET249.2
- new net N$998: J16.57, TET249.3
- new net N$999: J16.56, TET248.0
- new net REF12: J13.69, REF12.P$1
- new net REF13: J14.69, REF13.P$1
- new net REF14: J15.69, REF14.P$1
- new net REF15: J16.69, REF15.P$1
- net GND: now also GND2.P$1, GND24.P$1, GND25.P$1, GND26.P$1, GND27.P$1, GND28.P$1, GND29.P$1, GND30.P$1, J13.70, J14.70, J15.70, J16.70, SHLD_A12.P$1, SHLD_A13.P$1, SHLD_A14.P$1, SHLD_A15.P$1
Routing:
- net N$785: track 0.00 -> 8.94 mm, vias 0 -> 1
- net N$977: track 0.00 -> 8.94 mm, vias 0 -> 1
- net N$849: track 0.00 -> 8.94 mm, vias 0 -> 1
- net N$913: track 0.00 -> 8.94 mm, vias 0 -> 1
- net N$847: track 0.00 -> 8.77 mm, vias 0 -> 1
- net N$975: track 0.00 -> 8.77 mm, vias 0 -> 1
- net N$911: track 0.00 -> 8.77 mm, vias 0 -> 1
- net N$783: track 0.00 -> 8.77 mm, vias 0 -> 1
- net N$789: track 0.00 -> 8.58 mm, vias 0 -> 1
- net N$981: track 0.00 -> 8.58 mm, vias 0 -> 1
- net N$853: track 0.00 -> 8.58 mm, vias 0 -> 1
- net N$917: track 0.00 -> 8.58 mm, vias 0 -> 1
- net N$907: track 0.00 -> 8.33 mm, vias 0 -> 1
- net N$843: track 0.00 -> 8.33 mm, vias 0 -> 1
- net N$971: track 0.00 -> 8.33 mm, vias 0 -> 1
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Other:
- board size 70.6 x 58 mm -> 76.6 x 77.2 mm
